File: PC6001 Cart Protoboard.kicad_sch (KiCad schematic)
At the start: 20 parts, among them J1 PC-6001 edge connector, SW1 PicoReset, SW2 EspReset, SW3 Button A, U2 ESP32-DevKitC, U3 74LS32, U4 microSD-Breakout, U5 74LS08, U6 SN74LVC245AN, U7 SN74LVC245AN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

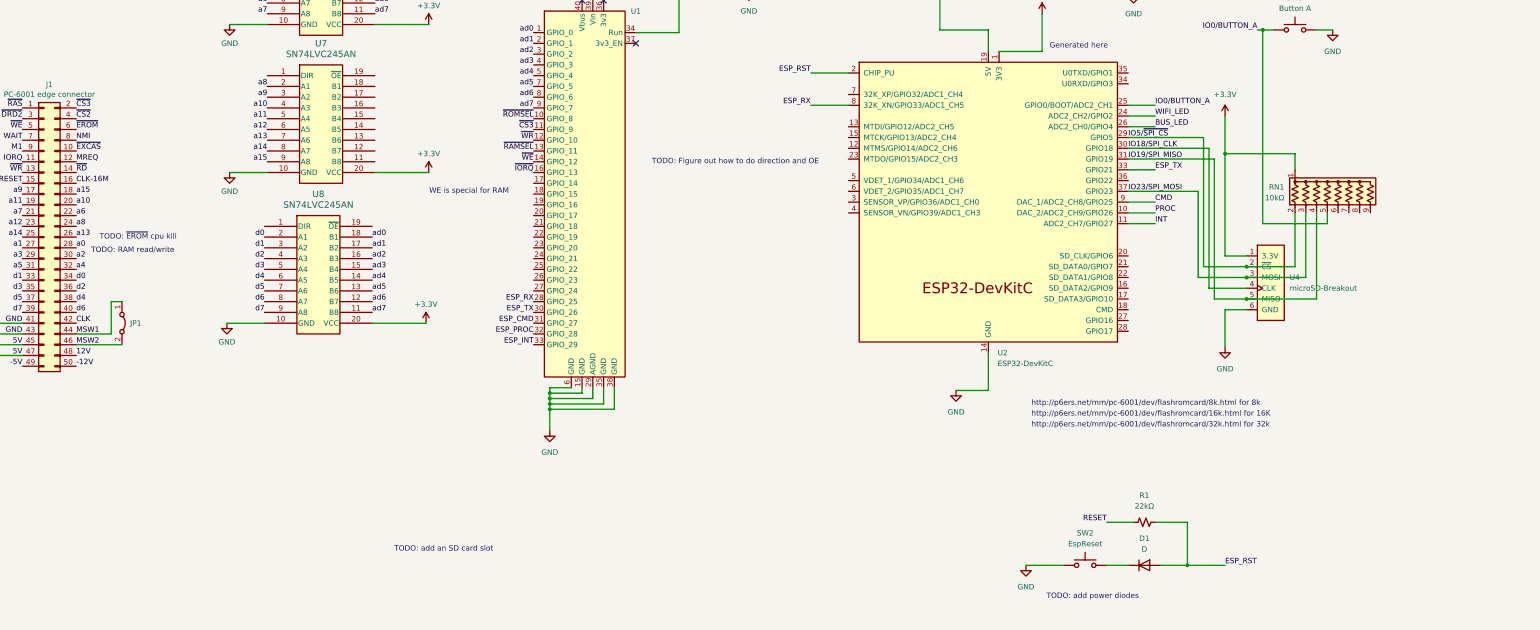
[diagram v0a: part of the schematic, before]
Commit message: Buffers starting, RAMWR not right
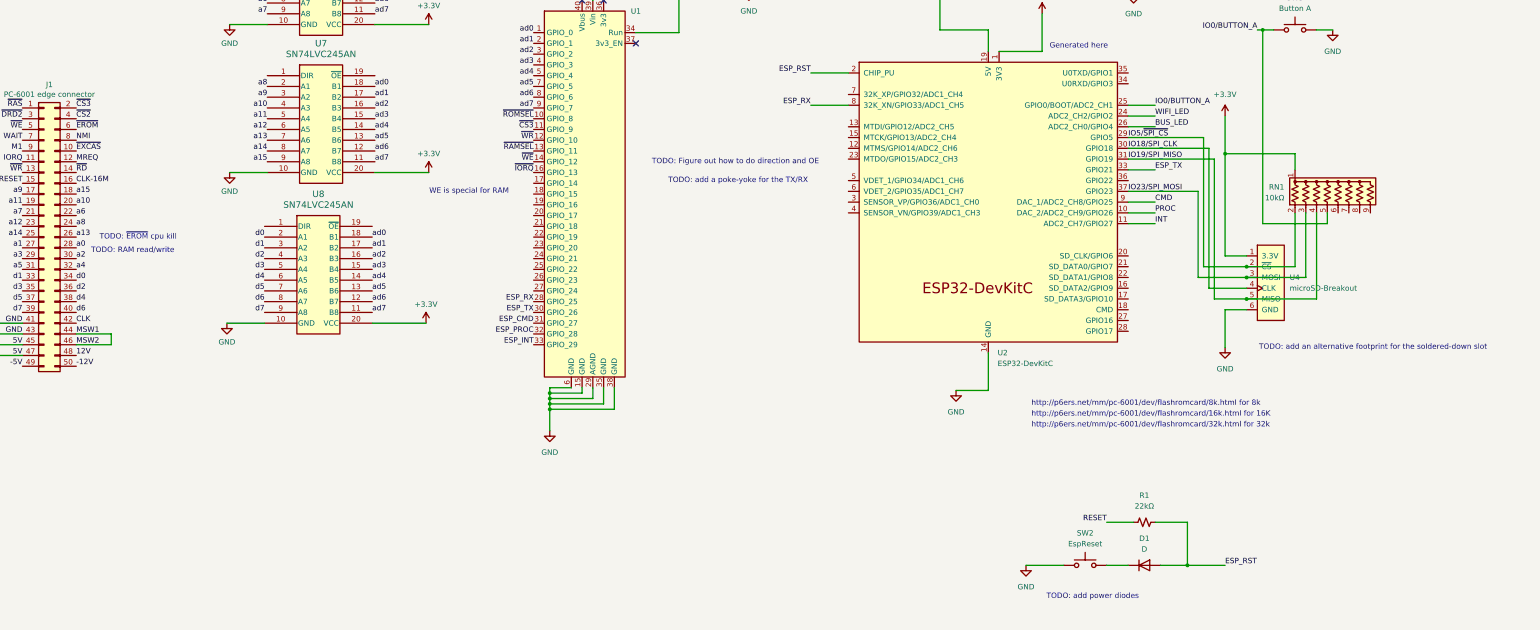
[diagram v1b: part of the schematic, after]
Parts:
- removed JP1: Jumper_2_Bridged, Jumper:SolderJumper-2_P1.3mm_Bridged2Bar_Pad1.0x1.5mm, symbol Jumper:Jumper_2_Bridged
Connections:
- net MSW2 is gone; now on net MSW1: J1.46 (Pin_46)
- net ad0: now also U7.18 (B1)
- net ad1: now also U7.17 (B2)
- net ad2: now also U7.16 (B3)
- net ad3: now also U7.15 (B4)
- net ad4: now also U7.14 (B5)
- net ad5: now also U7.13 (B6)
- net ad6: now also U7.12 (B7)
- net ad7: now also U7.11 (B8)
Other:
- note added: "TODO: add a poke-yoke for the TX/RX"
- note added: "TODO: add an alternative footprint for the soldered-down slot"
- note removed: "TODO: add an SD card slot"
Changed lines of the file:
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@@
 	(wire
 		(pts
-			(xy 72.39 132.08) (xy 72.39 124.46)
-		)
-		(stroke
-			(width 0)
-			(type default)
-		)
-	)
-	(wire
-		(pts
 			(xy 175.895 147.32) (xy 175.895 146.05)
 		)
@@
 	(wire
 		(pts
-			(xy 72.39 124.46) (xy 74.93 124.46)
+			(xy 332.74 123.825) (xy 340.36 123.825)
 		)
 		(stroke
@@
 	(wire
 		(pts
-			(xy 332.74 123.825) (xy 340.36 123.825)
+			(xy 64.135 134.62) (xy 72.39 134.62)
 		)
 		(stroke
@@
 	(wire
 		(pts
-			(xy 328.93 118.745) (xy 340.36 118.745)
+			(xy 72.39 134.62) (xy 72.39 132.08)
 		)
 		(stroke
@@
 	(wire
 		(pts
-			(xy 330.2 85.725) (xy 330.2 116.205)
+			(xy 328.93 118.745) (xy 340.36 118.745)
 		)
 		(stroke
@@
 	(wire
 		(pts
-			(xy 100.33 59.055) (xy 109.22 59.055)
+			(xy 330.2 85.725) (xy 330.2 116.205)
 		)
 		(stroke
@@
 	(wire
 		(pts
-			(xy 326.39 176.53) (xy 326.39 186.69)
+			(xy 100.33 59.055) (xy 109.22 59.055)
 		)
 		(stroke
@@
 	(wire
 		(pts
-			(xy 175.895 154.94) (xy 175.895 149.86)
+			(xy 326.39 176.53) (xy 326.39 186.69)
 		)
 		(stroke
@@
 	(wire
 		(pts
-			(xy 313.69 34.925) (xy 318.77 34.925)
+			(xy 175.895 154.94) (xy 175.895 149.86)
 		)
 		(stroke
@@
 	(wire
 		(pts
-			(xy 288.29 186.69) (xy 297.18 186.69)
+			(xy 313.69 34.925) (xy 318.77 34.925)
 		)
 		(stroke
@@
 	(wire
 		(pts
-			(xy 356.87 123.825) (xy 356.87 103.505)
+			(xy 288.29 186.69) (xy 297.18 186.69)
 		)
 		(stroke
@@
 	(wire
 		(pts
-			(xy 64.135 134.62) (xy 74.93 134.62)
+			(xy 356.87 123.825) (xy 356.87 103.505)
 		)
 		(stroke
@@
 		)
 	)
-	(text "TODO: add an SD card slot"
+	(text "TODO: add a poke-yoke for the TX/RX"
 		(exclude_from_sim no)
-		(at 150.876 182.88 0)
+		(at 220.345 95.885 0)
 		(effects
 			(font
@@
 		)
 	)
+	(text "TODO: add an alternative footprint for the soldered-down slot"
+		(exclude_from_sim no)
+		(at 370.205 135.255 0)
+		(effects
+			(font
+				(size 1.27 1.27)
+			)
+		)
+	)
 	(text "TODO: add power diodes"
 		(exclude_from_sim no)
@@
 		)
 	)
+	(label "ad0"
+		(at 134.62 73.66 0)
+		(fields_autoplaced yes)
+		(effects
+			(font
+				(size 1.27 1.27)
+			)
+			(justify left bottom)
+		)
+	)
 	(label "d7"
 		(at 108.585 127 180)
@@
 		)
 	)
+	(label "ad1"
+		(at 134.62 76.2 0)
+		(fields_autoplaced yes)
+		(effects
+			(font
+				(size 1.27 1.27)
+			)
+			(justify left bottom)
+		)
+	)
 	(label "a1"
 		(at 51.435 111.76 180)
@@
 		)
 	)
+	(label "ad5"
+		(at 134.62 86.36 0)
+		(fields_autoplaced yes)
+		(effects
+			(font
+				(size 1.27 1.27)
+			)
+			(justify left bottom)
+		)
+	)
 	(label "d3"
 		(at 108.585 116.84 180)
@@
 		)
 	)
+	(label "ad6"
+		(at 134.62 88.9 0)
+		(fields_autoplaced yes)
+		(effects
+			(font
+				(size 1.27 1.27)
+			)
+			(justify left bottom)
+		)
+	)
 	(label "a4"
 		(at 64.135 116.84 0)
@@
 		)
 	)
+	(label "ad7"
+		(at 134.62 91.44 0)
+		(fields_autoplaced yes)
+		(effects
+			(font
+				(size 1.27 1.27)
+			)
+			(justify left bottom)
+		)
+	)
 	(label "ad0"
 		(at 134.62 38.735 0)
@@
 		)
 	)
+	(label "ad3"
+		(at 134.62 81.28 0)
+		(fields_autoplaced yes)
+		(effects
+			(font
+				(size 1.27 1.27)
+			)
+			(justify left bottom)
+		)
+	)
 	(label "5V"
 		(at 51.435 137.16 180)
@@
 		)
 	)
+	(label "ad4"
+		(at 134.62 83.82 0)
+		(fields_autoplaced yes)
+		(effects
+			(font
+				(size 1.27 1.27)
+			)
+			(justify left bottom)
+		)
+	)
 	(label "IO0{slash}BUTTON_A"
 		(at 342.9 60.325 180)
@@
 		)
 	)
+	(label "ad2"
+		(at 134.62 78.74 0)
+		(fields_autoplaced yes)
+		(effects
+			(font
+				(size 1.27 1.27)
+			)
+			(justify left bottom)
+		)
+	)
 	(label "INT"
 		(at 318.77 106.045 0)
@@
 					(unit 1)
 				)
-			)
-		)
-	)
-	(symbol
-		(lib_id "Jumper:Jumper_2_Bridged")
-		(at 74.93 129.54 270)
-		(unit 1)
-		(exclude_from_sim no)
-		(in_bom yes)
-		(on_board yes)
-		(dnp no)
-		(fields_autoplaced yes)
-		(property "Reference" "JP1"
-			(at 76.835 129.54 90)
-			(effects
-				(font
-					(size 1.27 1.27)
-				)
-				(justify left)
-			)
-		)
-		(property "Value" "Jumper_2_Bridged"
-			(at 76.835 130.81 90)
-			(effects
-				(font
-					(size 1.27 1.27)
-				)
-				(justify left)
-				(hide yes)
-			)
-		)
-		(property "Footprint" "Jumper:SolderJumper-2_P1.3mm_Bridged2Bar_Pad1.0x1.5mm"
-			(at 74.93 129.54 0)
-			(effects
-				(font
-					(size 1.27 1.27)
-				)
-				(hide yes)
-			)
-		)
-		(property "Datasheet" "~"
-			(at 74.93 129.54 0)
-			(effects
-				(font
-					(size 1.27 1.27)
-				)
-				(hide yes)
-			)
-		)
-		(property "Description" ""
-			(at 74.93 129.54 0)
-			(effects
-				(font
-					(size 1.27 1.27)
-				)
-				(hide yes)
-			)
-		)
-		(pin "1"
-		)
-		(pin "2"
-		)
-		(instances
-			(project "PC6001 Cart Protoboard"
-				(path "/43e41326-819e-40e7-9c3a-9c7b5d01c509"
-					(reference "JP1")
-					(unit 1)
-				)

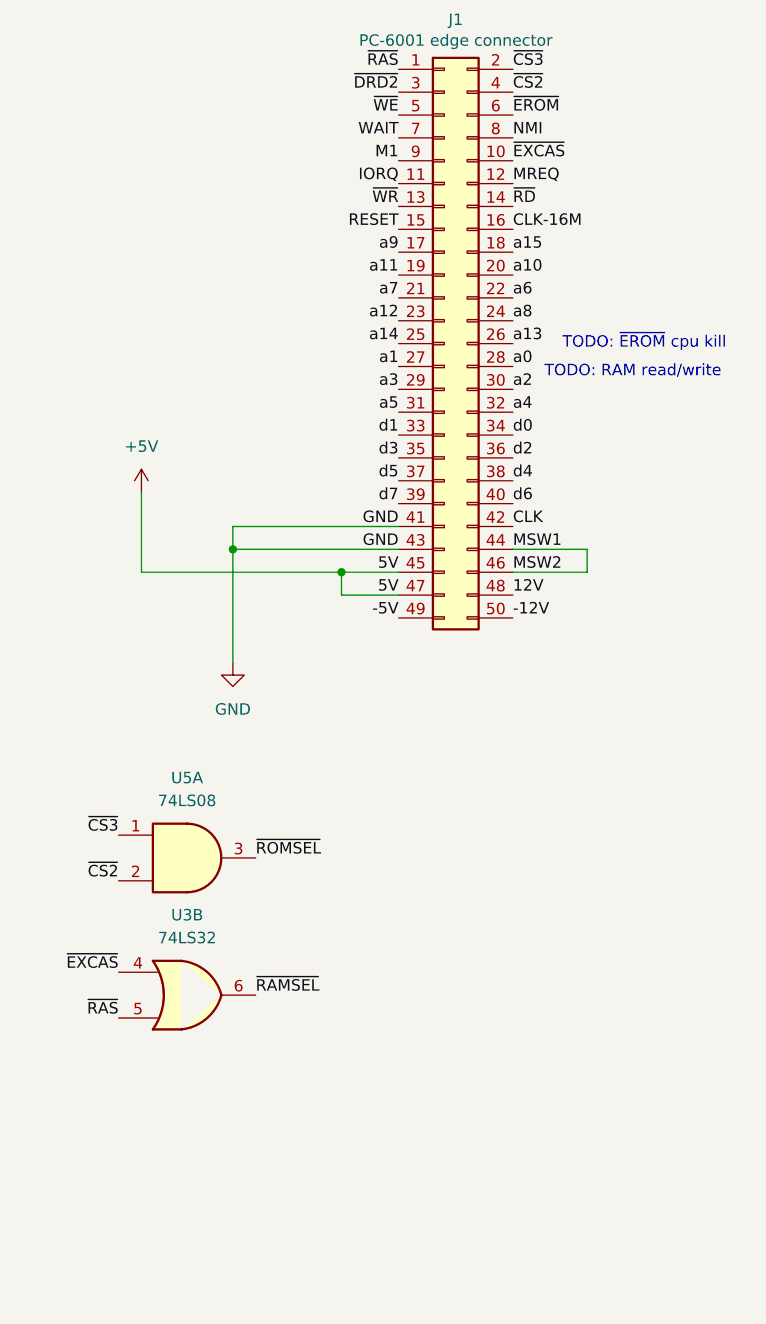
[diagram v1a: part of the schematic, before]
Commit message: Convenience signals to use up some gates
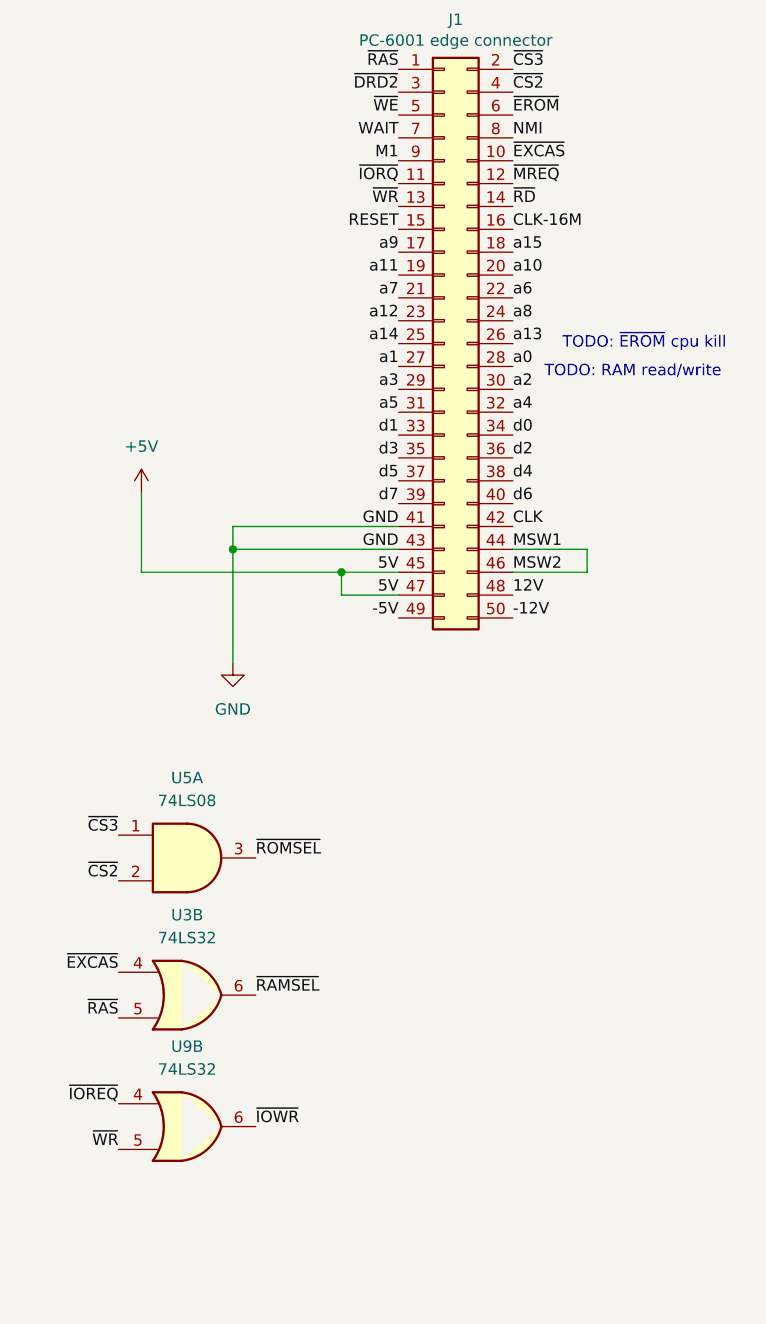
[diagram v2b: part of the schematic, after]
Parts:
- added U9: 74LS32, Package_DIP:DIP-14_W7.62mm_Socket_LongPads, symbol 74xx:74LS32
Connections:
- net IORQ is gone; now on net ~{IORQ}: J1.11 (Pin_11)
- net ~{WR}: now also U9.5
- net MREQ renamed ~{MREQ}
- new net ~{IOREQ}: U9.4
- new net ~{IOWR}: U9.6
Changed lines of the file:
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@@
 		)
 	)
+	(label "~{WR}"
+		(at 20.32 198.755 180)
+		(fields_autoplaced yes)
+		(effects
+			(font
+				(size 1.27 1.27)
+			)
+			(justify right bottom)
+		)
+	)
 	(label "a15"
 		(at 109.22 91.44 180)
@@
 		)
 	)
+	(label "~{IOWR}"
+		(at 35.56 196.215 0)
+		(fields_autoplaced yes)
+		(effects
+			(font
+				(size 1.27 1.27)
+			)
+			(justify left bottom)
+		)
+	)
 	(label "-5V"
 		(at 51.435 139.7 180)
@@
 		)
 	)
-	(label "IORQ"
+	(label "~{IORQ}"
 		(at 51.435 91.44 180)
 		(fields_autoplaced yes)
@@
 		)
 	)
-	(label "MREQ"
+	(label "~{MREQ}"
 		(at 64.135 91.44 0)
 		(fields_autoplaced yes)
@@
 		)
 	)
+	(label "~{IOREQ}"
+		(at 20.32 193.675 180)
+		(fields_autoplaced yes)
+		(effects
+			(font
+				(size 1.27 1.27)
+			)
+			(justify right bottom)
+		)
+	)
 	(label "a2"
 		(at 109.22 43.815 180)
@@
 				)
 			)
+		)
+	)
+	(symbol
+		(lib_id "74xx:74LS32")
+		(at 27.94 196.215 0)
+		(unit 2)
+		(exclude_from_sim no)
+		(in_bom yes)
+		(on_board yes)
+		(dnp no)
+		(fields_autoplaced yes)
+		(property "Reference" "U9"
+			(at 27.94 187.325 0)
+			(effects
+				(font
+					(size 1.27 1.27)
+				)
+			)
+		)
+		(property "Value" "74LS32"
+			(at 27.94 189.865 0)
+			(effects
+				(font
+					(size 1.27 1.27)
+				)
+			)
+		)
+		(property "Footprint" "Package_DIP:DIP-14_W7.62mm_Socket_LongPads"
+			(at 27.94 196.215 0)
+			(effects
+				(font
+					(size 1.27 1.27)
+				)
+				(hide yes)
+			)
+		)
+		(property "Datasheet" "http://www.ti.com/lit/gpn/sn74LS32"
+			(at 27.94 196.215 0)
+			(effects
+				(font
+					(size 1.27 1.27)
+				)
+				(hide yes)
+			)
+		)
+		(property "Description" "Quad 2-input OR"
+			(at 27.94 196.215 0)
+			(effects
+				(font
+					(size 1.27 1.27)
+				)
+				(hide yes)
+			)
+		)
+		(pin "6"
+		)
+		(pin "11"
+		)
+		(pin "1"
+		)
+		(pin "13"
+		)
+		(pin "10"
+		)
+		(pin "2"
+		)
+		(pin "9"
+		)
+		(pin "8"
+		)
+		(pin "7"
+		)
+		(pin "5"
+		)
+		(pin "12"
+		)
+		(pin "3"
+		)
+		(pin "14"
+		)
+		(pin "4"
+		)
+		(instances
+			(project "PC6001 Cart Protoboard"
+				(path "/43e41326-819e-40e7-9c3a-9c7b5d01c509"
+					(reference "U9")
+					(unit 2)
+				)
+			)
